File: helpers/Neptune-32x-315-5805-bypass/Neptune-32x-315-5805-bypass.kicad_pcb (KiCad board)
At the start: 2 copper layers, 16.5 x 22.5 mm, 1 part, among them IC1 315-5805

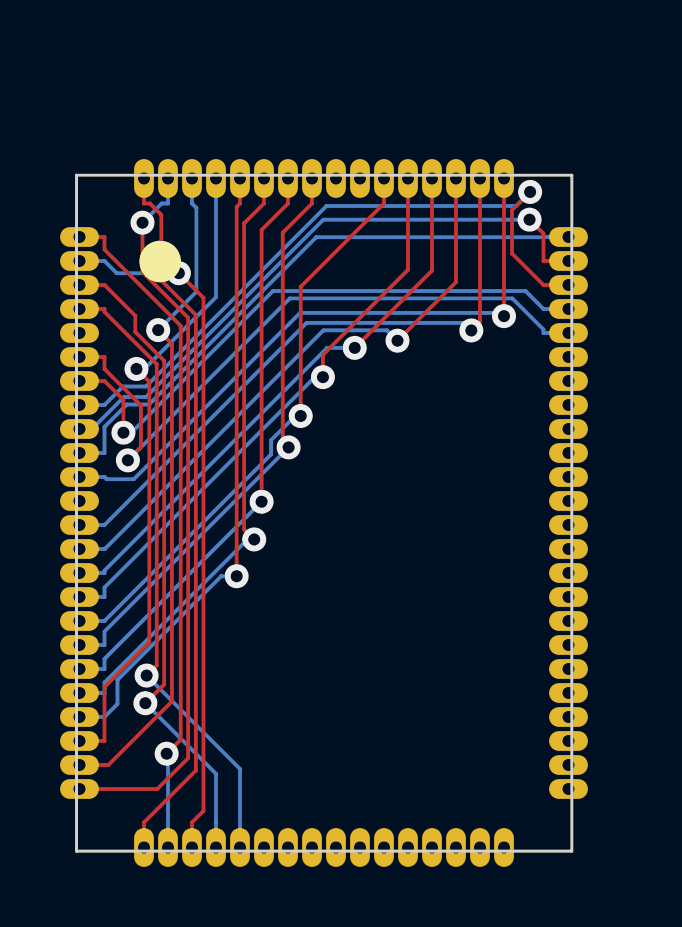
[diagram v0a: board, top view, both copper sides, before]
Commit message: Chnaged helper PCB's to be flex instead
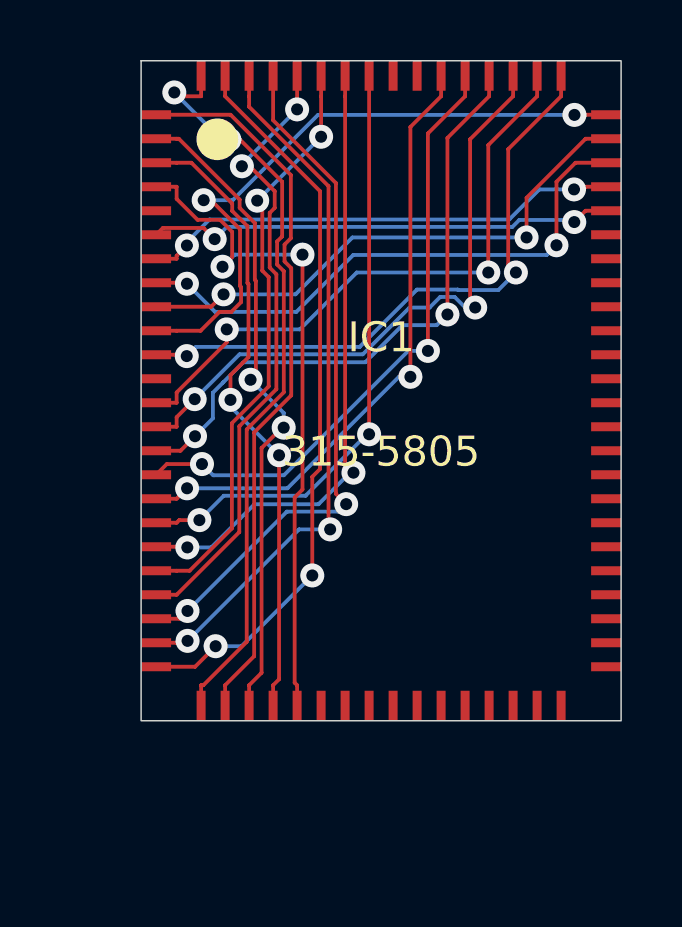
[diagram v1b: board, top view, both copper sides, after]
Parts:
- moved IC1 4.50 mm to (105.1, 73.7)
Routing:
- net VA23: track 22.4 -> 15.7 mm, vias 1 -> 2
- net VA21: track 22.6 -> 18.7 mm, vias 1 -> 2
- net VA22: track 19.9 -> 16.1 mm, vias 1 -> 2
- net VA20: track 20.3 -> 18.1 mm, vias 1 -> 2
- net VA19: track 19.8 -> 21.9 mm, vias 0 -> 2
- net VA1: track 20.9 -> 22.7 mm, vias 1 -> 2
- net VA4: track 22.4 -> 24.1 mm, vias 1 -> 0
- net VA14: track 19.1 -> 20.8 mm, vias 1 -> 2
- net VA15: track 19.0 -> 20.6 mm, vias 1 -> 2
- net VA8: track 21.6 -> 23.2 mm, vias 1 -> 2
- net VA7: track 22.2 -> 23.6 mm, vias 1 -> 2
- net VA5: track 23.9 -> 25.3 mm, vias 0 -> 2
- net VA3: track 23.1 -> 21.8 mm, vias 1 -> 2
- net VA11: track 19.7 -> 21.0 mm, vias 1 -> 2
- net VA16: track 20.0 -> 21.2 mm, vias 1 -> 2
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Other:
- board size 16.5 x 22.5 mm -> 16 x 22 mm
